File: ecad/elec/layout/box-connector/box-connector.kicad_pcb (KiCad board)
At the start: 2 copper layers, 225.7 x 100.8 mm, 0 parts

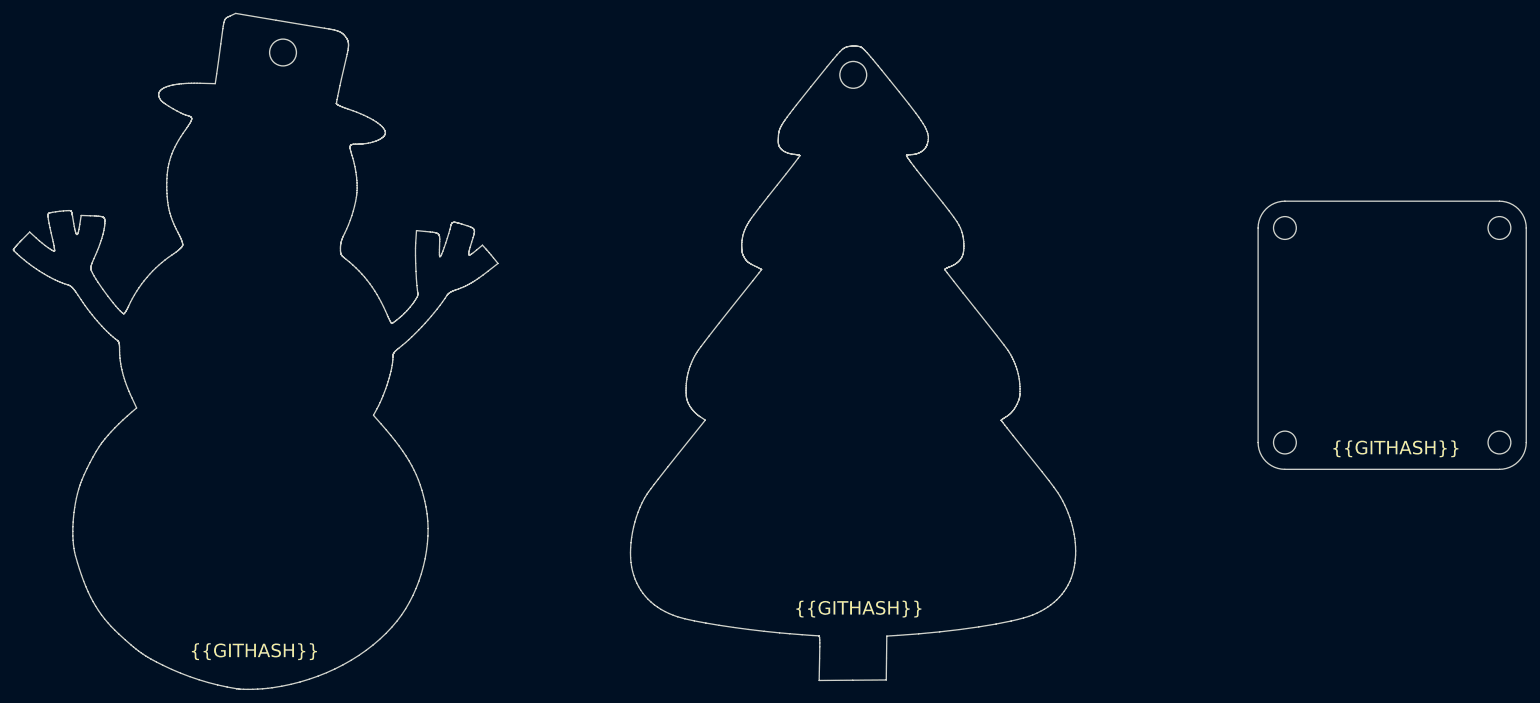
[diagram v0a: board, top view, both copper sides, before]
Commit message: remove and ignore kicad_prl files
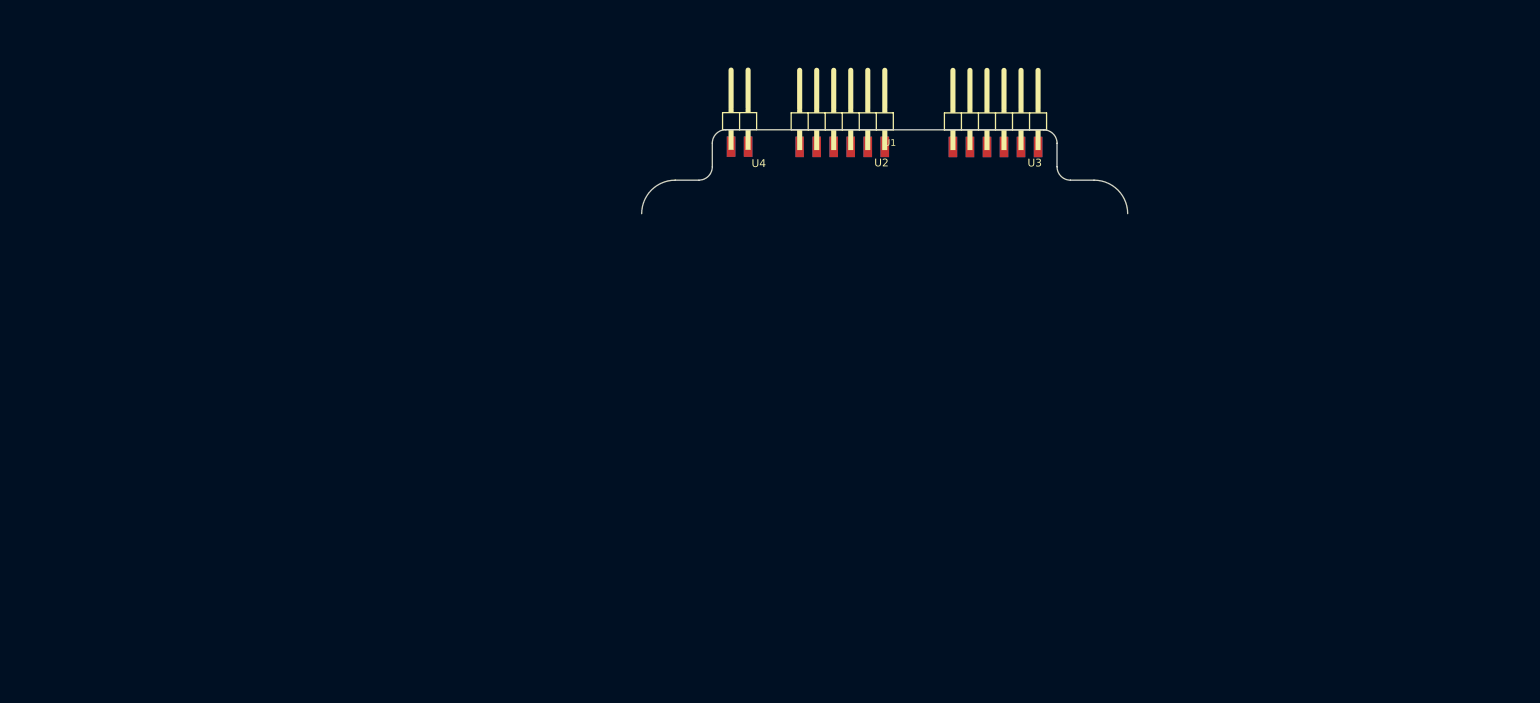
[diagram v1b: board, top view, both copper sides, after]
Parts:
- added U1: , lib:BOX_EMU, F.Cu at (166.7, 69.6)
- added U2: , lib:2X06_EDGE_REVERSED, F.Cu at (159.6, 73.2)
- added U3: , lib:2X06_EDGE_REVERSED, F.Cu at (182.4, 73.3)
- added U4: , lib:2X02_EDGE_REVERSED, F.Cu at (144.3, 66.9)
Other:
- board size 225.7 x 100.8 mm -> 72.5 x 12.5 mm
- board text removed: "{{GITHASH}}"
